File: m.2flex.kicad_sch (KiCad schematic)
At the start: 2 parts, among them CN4 DF40C-40DS-0.4V, CN6 DF40C-40DS-0.4V

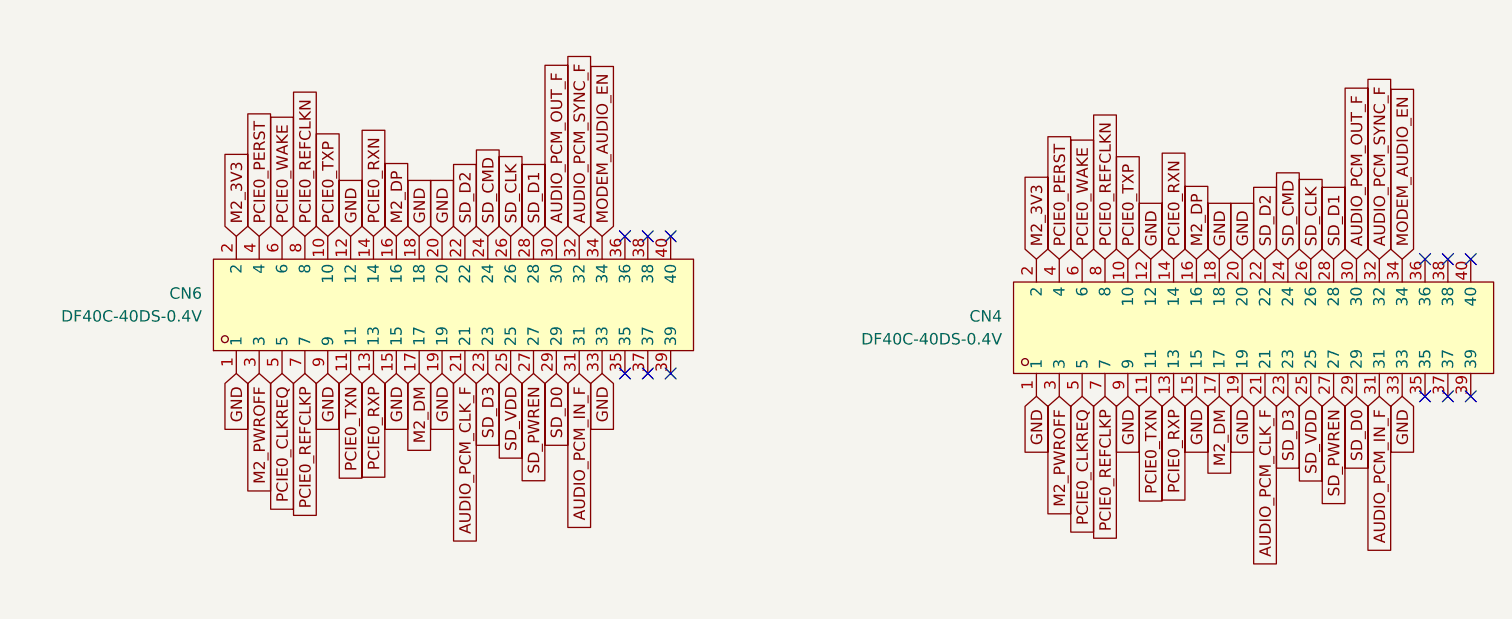
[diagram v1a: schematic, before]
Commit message: imported footprints and 3d models, replaced obsolete components, finished schematic audit, wired new usb hub and flash chip + more, removed stale nets
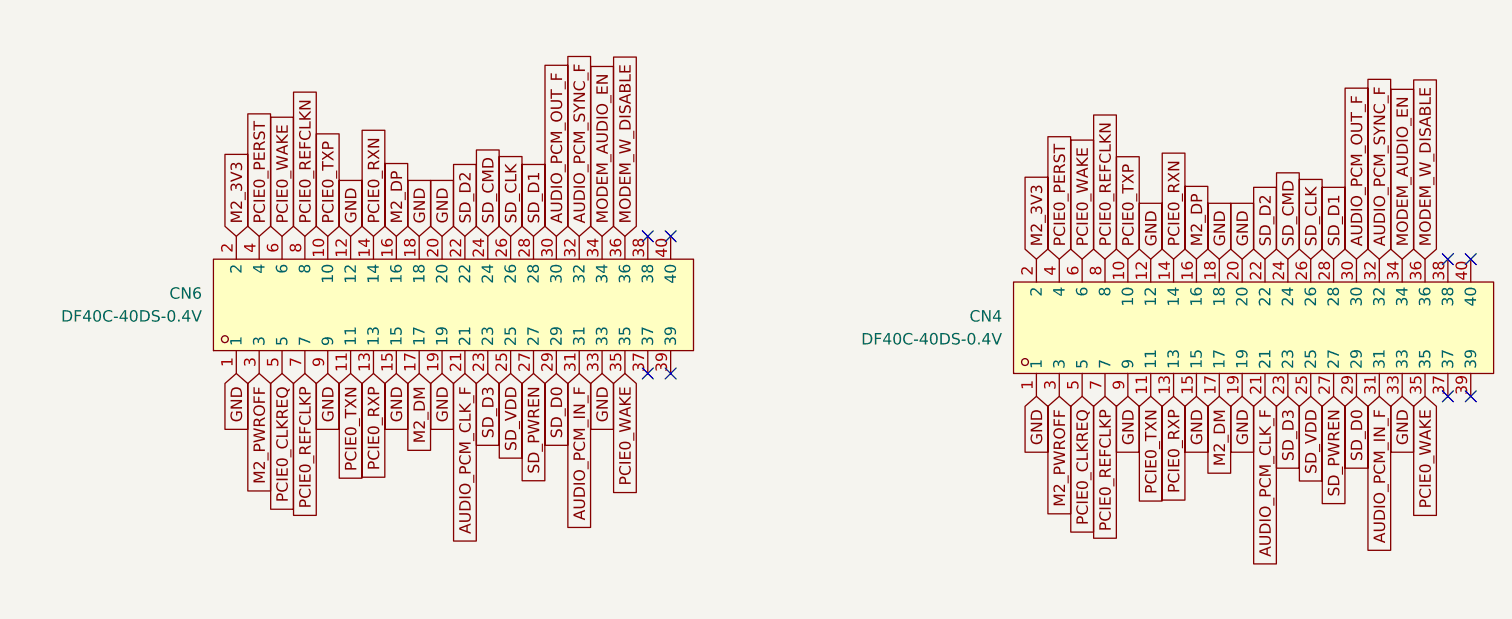
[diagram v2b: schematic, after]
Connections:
- net PCIE0_WAKE: now also CN4.35, CN6.35
- net MODEM_W_DISABLE: now reaches CN6.36
- net MODEM_W_DISABLE: now also CN4.36
- no-connect marks 12 -> 8
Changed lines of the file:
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@@
-	)
-	(no_connect
-		(at 175.26 73.66)
 	)
 	(no_connect
@@
 	)
 	(no_connect
-		(at 175.26 58.42)
-	)
-	(no_connect
 		(at 180.34 58.42)
-	)
-	(no_connect
-		(at 86.36 71.12)
 	)
 	(no_connect
@@
 		(at 177.8 58.42)
 	)
-	(no_connect
-		(at 86.36 55.88)
-	)
 	(global_label "M2_DP"
 		(shape input)
@@
 		)
 	)
+	(global_label "PCIE0_WAKE"
+		(shape input)
+		(at 175.26 73.66 270)
+		(fields_autoplaced yes)
+		(effects
+			(font
+				(size 1.27 1.27)
+			)
+			(justify right)
+		)
+		(property "Intersheetrefs" "${INTERSHEET_REFS}"
+			(at 175.26 88.0751 90)
+			(hide yes)
+			(show_name no)
+			(do_not_autoplace no)
+			(effects
+				(font
+					(size 1.27 1.27)
+				)
+				(justify right)
+			)
+		)
+	)
 	(global_label "GND"
 		(shape input)
@@
 		)
 	)
+	(global_label "MODEM_W_DISABLE"
+		(shape input)
+		(at 86.36 55.88 90)
+		(fields_autoplaced yes)
+		(effects
+			(font
+				(size 1.27 1.27)
+			)
+			(justify left)
+		)
+		(property "Intersheetrefs" "${INTERSHEET_REFS}"
+			(at 86.36 35.2359 90)
+			(hide yes)
+			(show_name no)
+			(do_not_autoplace no)
+			(effects
+				(font
+					(size 1.27 1.27)
+				)
+				(justify left)
+			)
+		)
+	)
 	(global_label "PCIE0_REFCLKP"
 		(shape input)
@@
 		)
 	)
+	(global_label "PCIE0_WAKE"
+		(shape input)
+		(at 86.36 71.12 270)
+		(fields_autoplaced yes)
+		(effects
+			(font
+				(size 1.27 1.27)
+			)
+			(justify right)
+		)
+		(property "Intersheetrefs" "${INTERSHEET_REFS}"
+			(at 86.36 85.5351 90)
+			(hide yes)
+			(show_name no)
+			(do_not_autoplace no)
+			(effects
+				(font
+					(size 1.27 1.27)
+				)
+				(justify right)
+			)
+		)
+	)
 	(global_label "M2_PWROFF"
 		(shape input)
@@
 			)
 		)
+	)
+	(global_label "MODEM_W_DISABLE"
+		(shape input)
+		(at 175.26 58.42 90)
+		(fields_autoplaced yes)
+		(effects
+			(font
+				(size 1.27 1.27)
+			)
+			(justify left)
+		)
+		(property "Intersheetrefs" "${INTERSHEET_REFS}"
+			(at 175.26 37.7759 90)
+			(hide yes)
+			(show_name no)
+			(do_not_autoplace no)
+			(effects
+				(font
+					(size 1.27 1.27)
+				)
+				(justify left)
+			)
+		)

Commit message: continued work on carrier board, started work on m.2 board
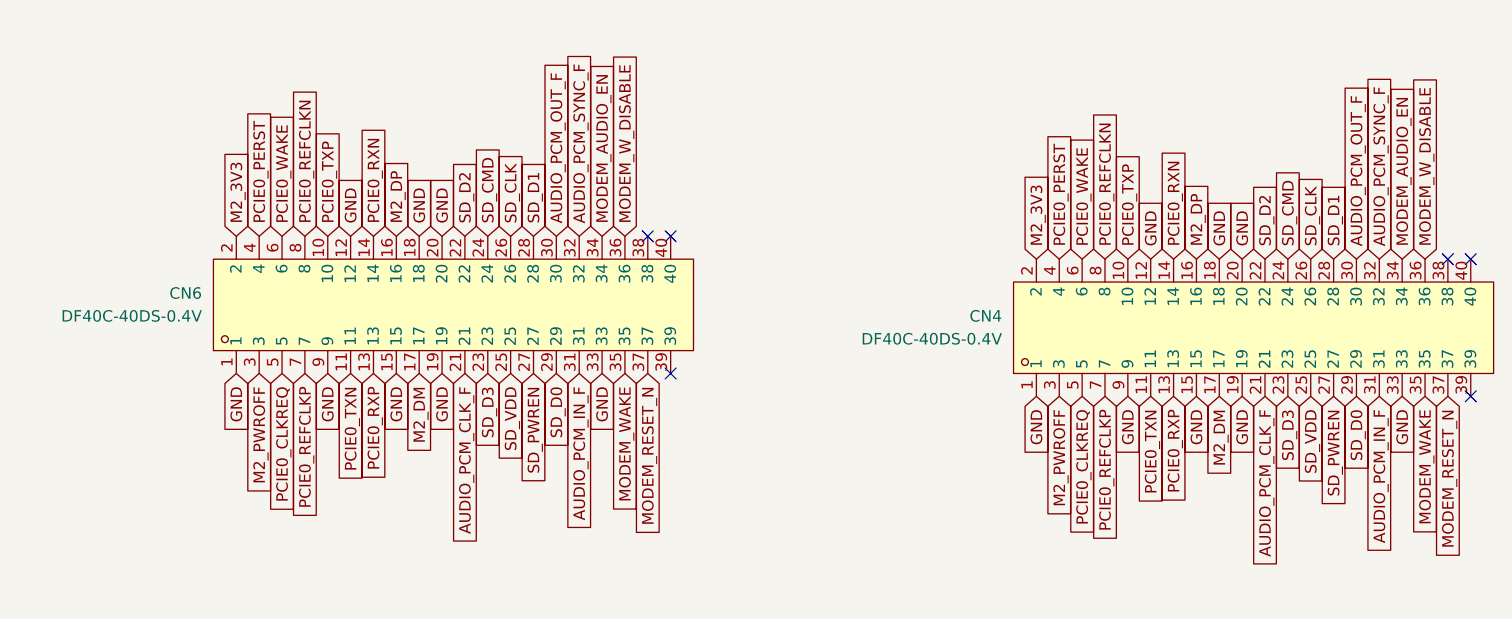
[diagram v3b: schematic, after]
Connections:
- net PCIE0_WAKE: no longer CN4.35, CN6.35
- net MODEM_RESET_N: now reaches CN6.37
- net MODEM_RESET_N: now also CN4.37
- new net MODEM_WAKE: CN4.35, CN6.35
- no-connect marks 8 -> 6

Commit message: finished m.2 board and copper pours, completed antenna bracket and power board, finished slateconnect board, reorganized libraries
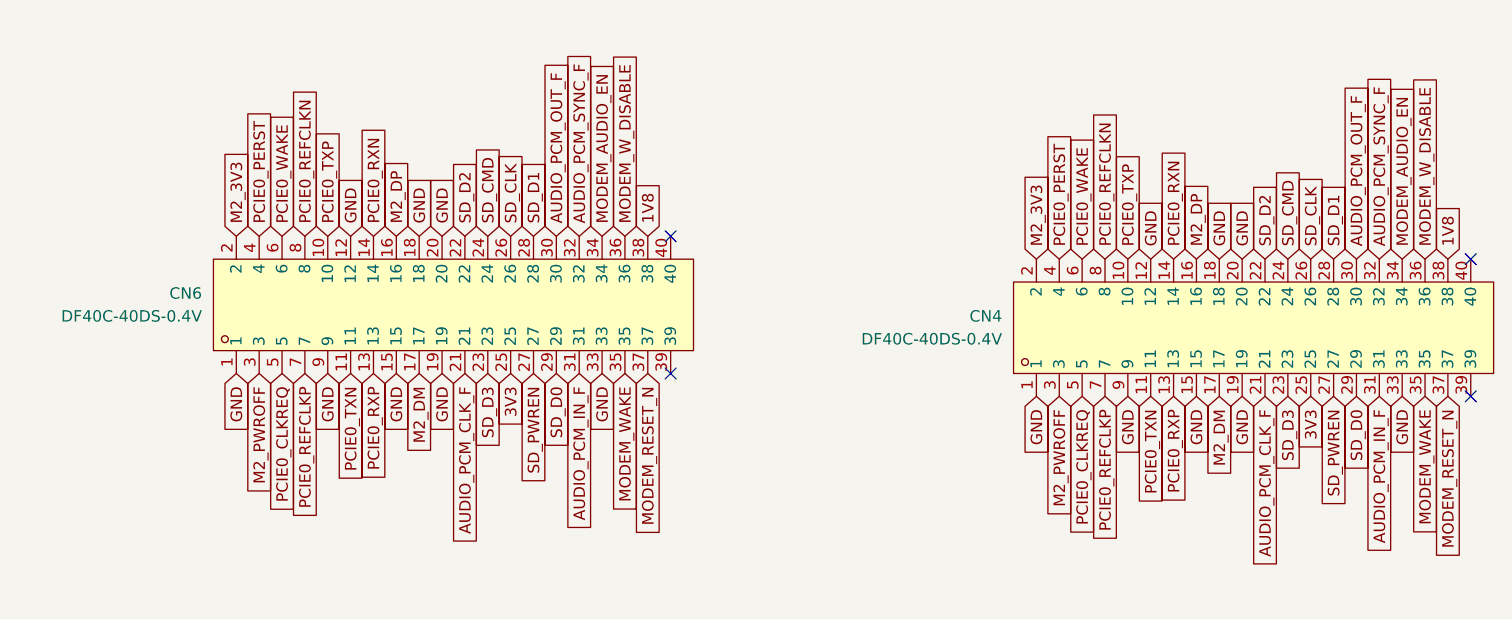
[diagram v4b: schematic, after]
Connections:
- net 1V8: now reaches CN6.38
- net 1V8: now also CN4.38
- net SD_VDD renamed 3V3
- no-connect marks 6 -> 4
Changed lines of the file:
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@@
-	)
-	(no_connect
-		(at 88.9 55.88)
 	)
 	(no_connect
 		(at 180.34 73.66)
 	)
-	(no_connect
-		(at 177.8 58.42)
-	)
 	(global_label "M2_DP"
 		(shape input)
@@
 		)
 	)
+	(global_label "1V8"
+		(shape input)
+		(at 88.9 55.88 90)
+		(fields_autoplaced yes)
+		(effects
+			(font
+				(size 1.27 1.27)
+			)
+			(justify left)
+		)
+		(property "Intersheetrefs" "${INTERSHEET_REFS}"
+			(at 88.9 49.3872 90)
+			(hide yes)
+			(show_name no)
+			(do_not_autoplace no)
+			(effects
+				(font
+					(size 1.27 1.27)
+				)
+				(justify left)
+			)
+		)
+	)
 	(global_label "PCIE0_CLKREQ"
 		(shape input)
@@
 		)
 	)
-	(global_label "SD_VDD"
+	(global_label "3V3"
 		(shape input)
 		(at 73.66 71.12 270)
@@
 		)
 		(property "Intersheetrefs" "${INTERSHEET_REFS}"
-			(at 73.66 81.1809 90)
+			(at 73.66 77.6128 90)
 			(hide yes)
 			(show_name no)
@@
 		)
 	)
+	(global_label "1V8"
+		(shape input)
+		(at 177.8 58.42 90)
+		(fields_autoplaced yes)
+		(effects
+			(font
+				(size 1.27 1.27)
+			)
+			(justify left)
+		)
+		(property "Intersheetrefs" "${INTERSHEET_REFS}"
+			(at 177.8 51.9272 90)
+			(hide yes)
+			(show_name no)
+			(do_not_autoplace no)
+			(effects
+				(font
+					(size 1.27 1.27)
+				)
+				(justify left)
+			)
+		)
+	)
 	(global_label "M2_PWROFF"
 		(shape input)
@@
 		)
 	)
-	(global_label "SD_VDD"
+	(global_label "3V3"
 		(shape input)
 		(at 162.56 73.66 270)
@@
 		)
 		(property "Intersheetrefs" "${INTERSHEET_REFS}"
-			(at 162.56 83.7209 90)
-			(hide yes)
-			(show_name no)
+			(at 162.56 80.1528 90)
+			(hide yes)
+			(show_name no)
